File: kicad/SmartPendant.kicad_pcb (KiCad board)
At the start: 2 copper layers, 125 x 59 mm, 51 parts, among them J1 UART, J2 ST-LINK, J3 Encoder, J5 Display, J6 USB_C_Receptacle_USB2.0_16P, J8 Micro_SD_Card_Det1, Q1 MMBT3904, U1 WEACT BLACKPILL F4X1, U2 AMS1117-3.3, U3 MB85RC256VPNF-G-JNERE1

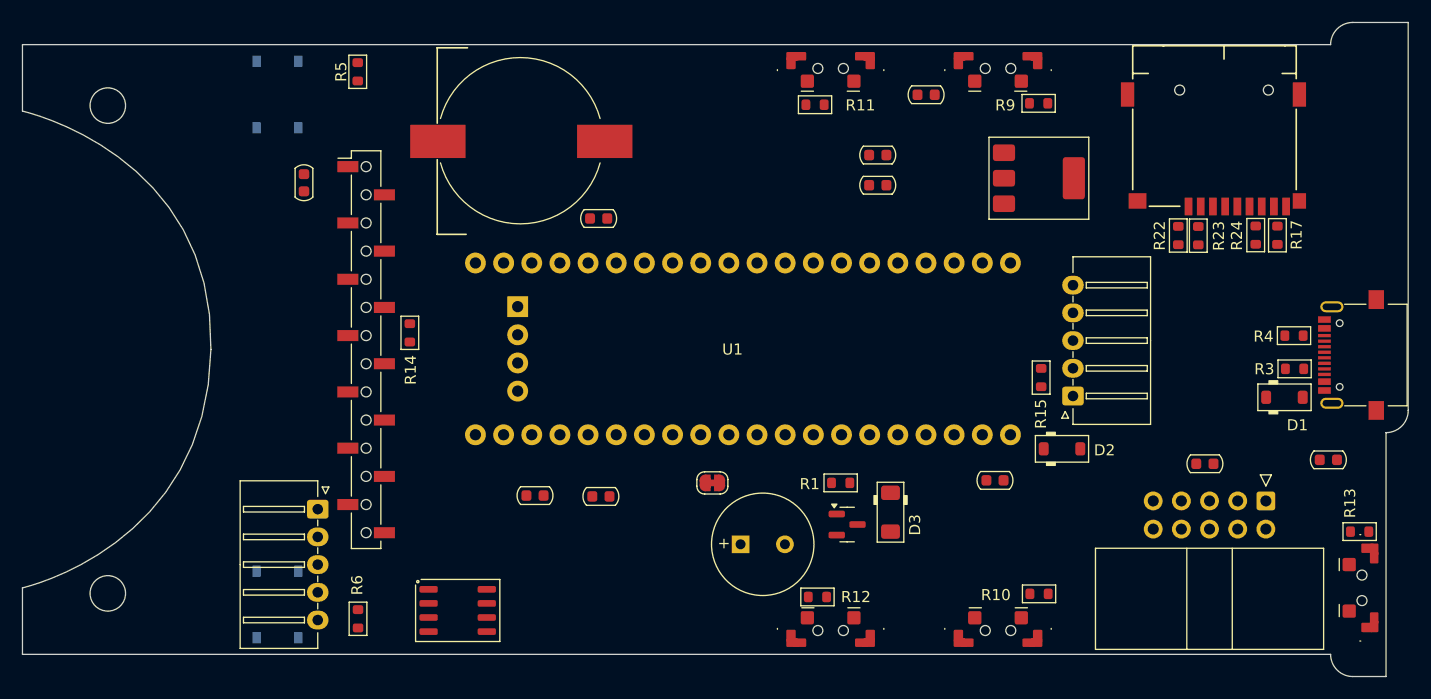
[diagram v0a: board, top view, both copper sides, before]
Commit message: Make PCB wider.
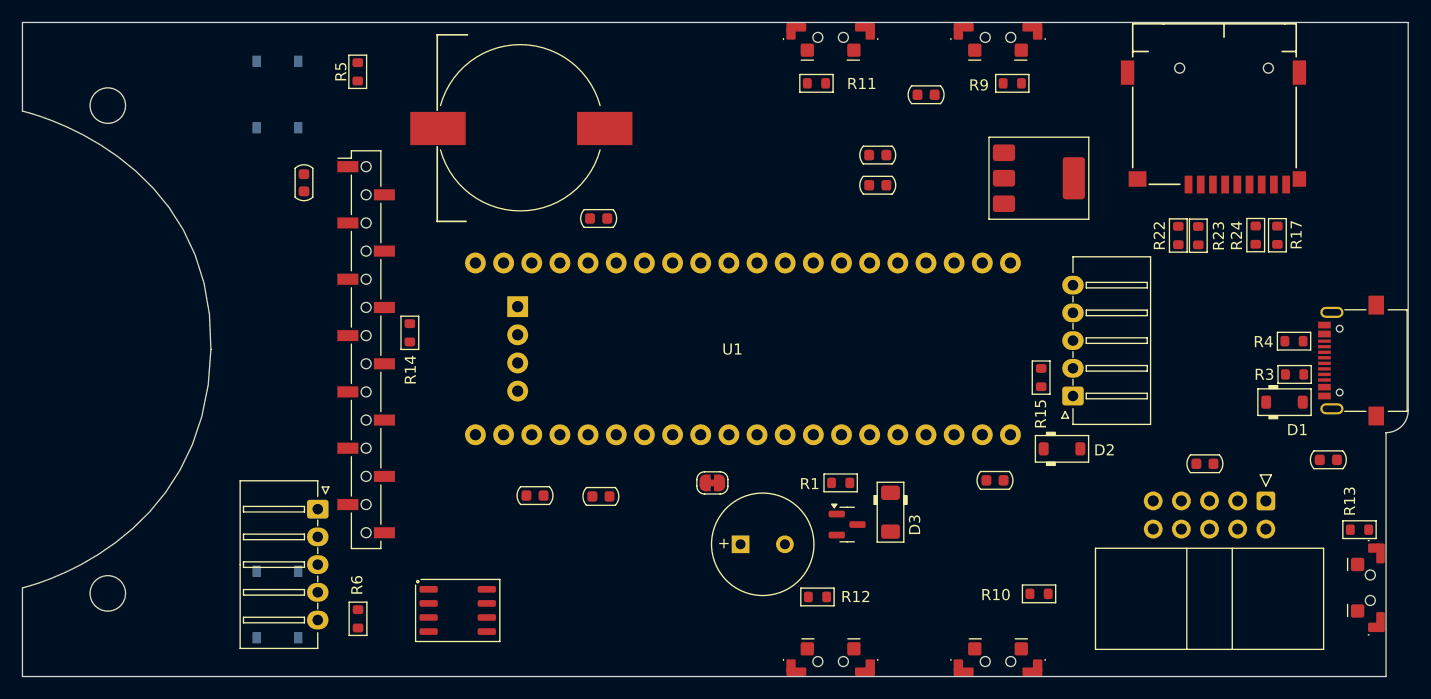
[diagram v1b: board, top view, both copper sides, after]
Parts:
- moved R9 2.98 mm to (214.3, 53.5)
- moved BTN_RD1 2.80 mm to (197.9, 104.9)
- moved BTN_RU1 2.80 mm to (213.0, 104.9)
- moved BTN_LD1 2.80 mm to (197.9, 50.1)
- moved BTN_LU1 2.80 mm to (213.0, 50.1)
- moved J8 1.98 mm to (233.4, 55.6)
- moved R11 1.93 mm to (196.6, 53.5)
- moved BT1 1.17 mm to (169.9, 57.5)
- moved BTN_USR1 0.75 mm to (245.8, 99.0)
- moved R3 0.50 mm to (239.8, 79.8)
- moved J6 0.50 mm to (246.1, 78.5)
- moved R4 0.50 mm to (239.7, 76.8)
- moved D1 0.44 mm to (238.8, 82.2)
- moved R13 0.18 mm to (245.6, 93.8)
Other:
- outline, holes or cut-outs redrawn

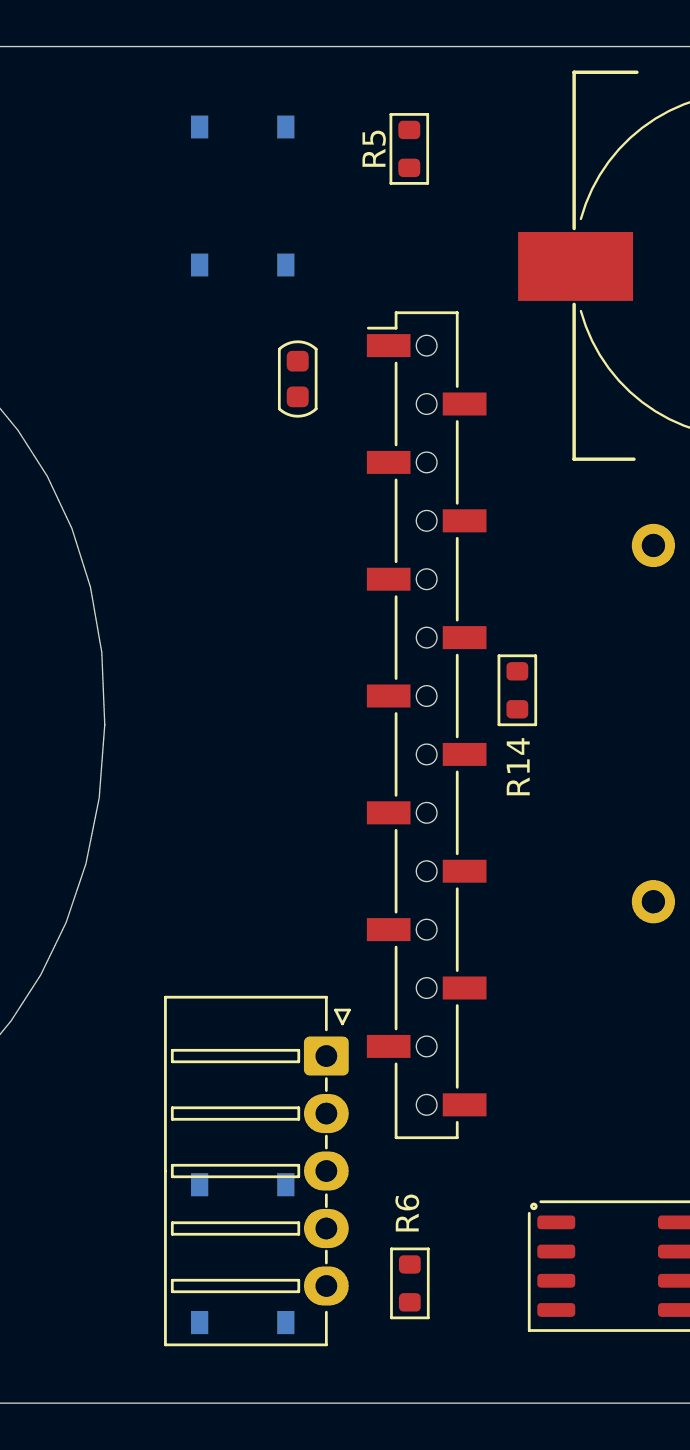
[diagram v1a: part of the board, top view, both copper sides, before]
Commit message: Change front buttons.
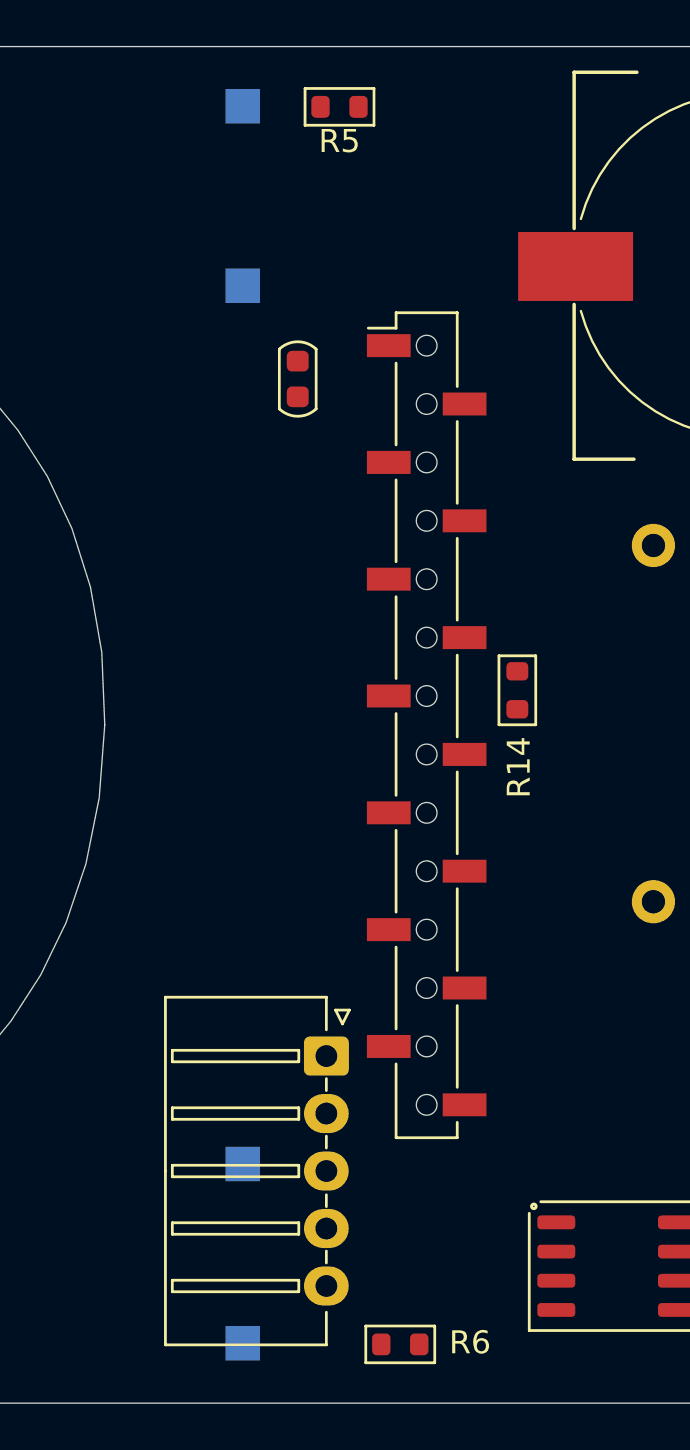
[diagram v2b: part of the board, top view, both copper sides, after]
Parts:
- BTN_L1, BTN_R1: footprint Button_Switch_SMD:SW_Push_1P1T_XKB_TS-1187A -> Button_Switch_SMD:SW_SPST_CK_RS282G05A3
- moved R5 3.54 mm to (152.2, 50.6), turned to 180 degrees
- moved R6 2.69 mm to (154.9, 104.4), turned to 180 degrees
- turned BTN_R1 to 90 degrees

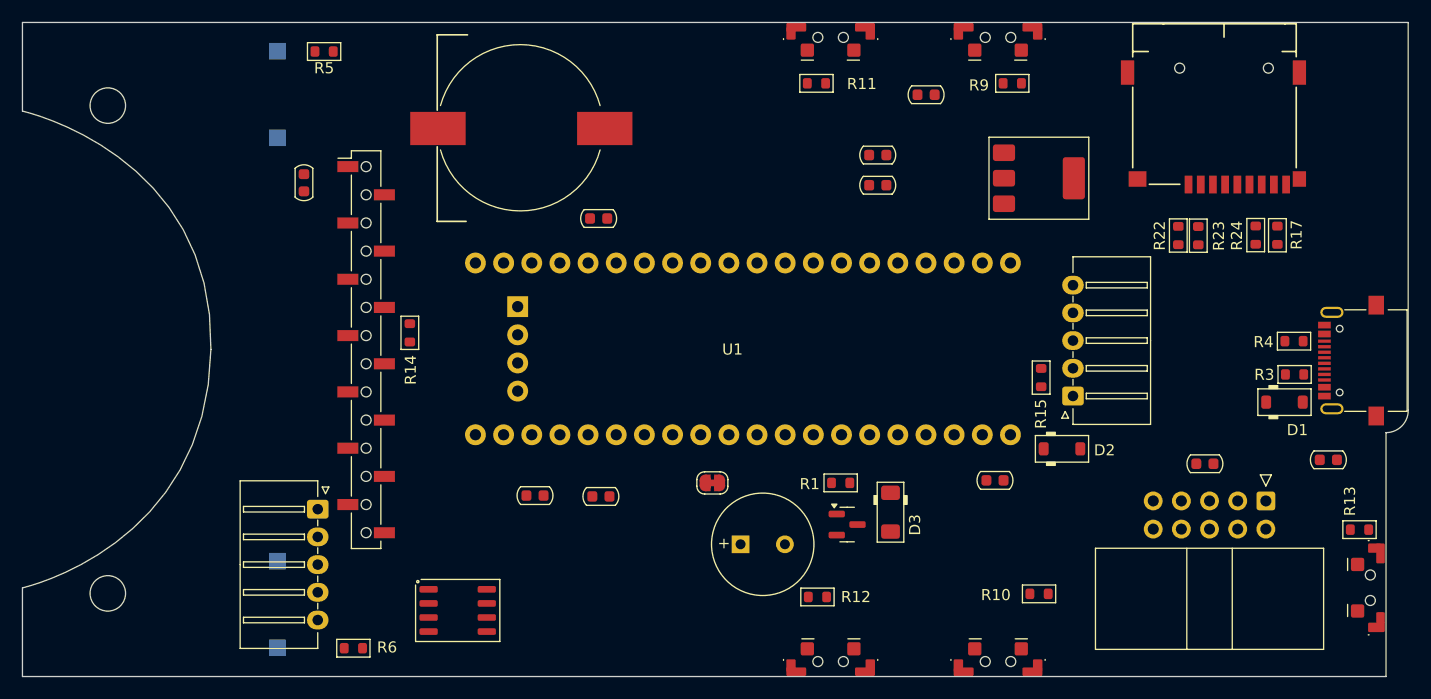
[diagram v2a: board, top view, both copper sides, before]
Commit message: Correct last footprints.
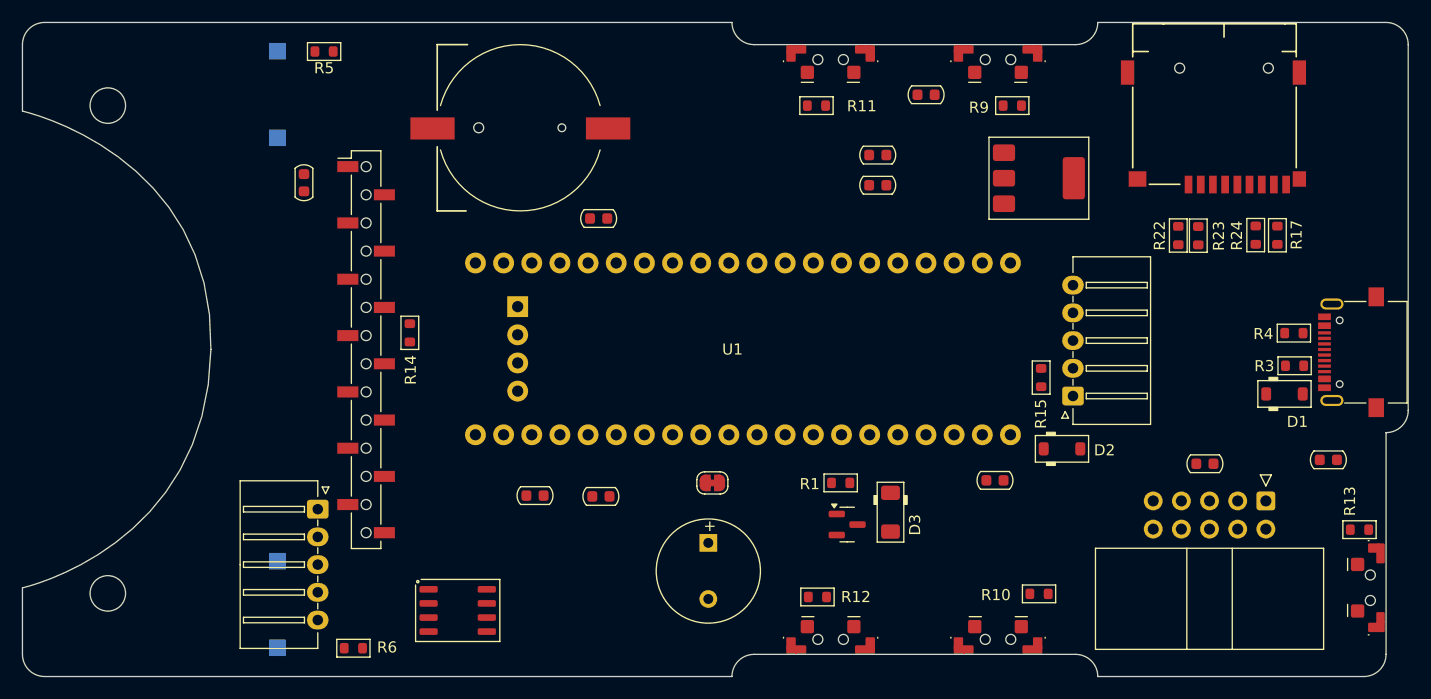
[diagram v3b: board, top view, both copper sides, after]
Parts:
- BZ1: footprint Buzzer_Beeper:MagneticBuzzer_PUI_AT-0927-TT-6-R -> Custom:Buzzer_4.7x9.4mm
- moved BZ1 2.91 mm to (186.9, 94.9), turned to -90 degrees
- moved R11 2.01 mm to (196.6, 55.5)
- moved R9 2.01 mm to (214.3, 55.5)
- moved BTN_LD1 2.00 mm to (197.9, 52.1)
- moved BTN_LU1 2.00 mm to (213.0, 52.1)
- moved BTN_RD1 2.00 mm to (197.9, 102.9)
- moved BTN_RU1 2.00 mm to (213.0, 102.9)
- moved R3 0.78 mm to (239.8, 79.0)
- moved J6 0.75 mm to (246.1, 77.8)
- moved D1 0.74 mm to (238.8, 81.5)
- moved R4 0.73 mm to (239.7, 76.0)
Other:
- outline, holes or cut-outs redrawn
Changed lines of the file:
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@@
 	(footprint "Custom:SMD_Push_Side_button_3x6x3.5mm"
 		(layer "F.Cu")
-		(at 197.9 50.1 180)
+		(at 197.9 52.1 180)
 		(descr "Microminiature SMT Side Actuated, 4.2 x 2.8 x 1.42mm with pegs, https://www.ckswitches.com/media/1482/kms.pdf")
 		(tags "Switch SPST KMS2")
@@
 	(footprint "PCM_Resistor_SMD_AKL:R_0603_1608Metric"
 		(layer "F.Cu")
-		(at 239.6998 76.75 180)
+		(at 239.6876 76.0222 180)
 		(descr "Resistor SMD 0603 (1608 Metric), square (rectangular) end terminal, IPC_7351 nominal, (Body size source: IPC-SM-782 page 72, https://www.pcb-3d.com/wordpress/wp-content/uploads/ipc-sm-782a_amendment_1_and_2.pdf), Alternate KiCad Library")
 		(tags "resistor")
@@
 	(footprint "Custom:USB_C_Receptacle_AliExpress_16pin"
 		(layer "F.Cu")
-		(at 246.1166 78.5 90)
+		(at 246.1166 77.75 90)
 		(descr "USB Type C, right-angle, SMT, https://datasheet.lcsc.com/szlcsc/1811141824_XKB-Enterprise-U262-161N-4BVC11_C319148.pdf")
 		(tags "USB C Type-C Receptacle SMD")
@@
 		)
 	)
-	(footprint "Buzzer_Beeper:MagneticBuzzer_PUI_AT-0927-TT-6-R"
+	(footprint "Custom:Buzzer_4.7x9.4mm"
 		(layer "F.Cu")
-		(at 189.7766 95.0722)
+		(at 186.8678 94.9452 -90)
 		(descr "Buzzer Magnetic 9mm AT-0927-TT-6-R, http://www.puiaudio.com/pdf/AT-0927-TT-6-R.pdf")
 		(tags "Buzzer Magnetic 9mm AT-0927-TT-6-R")
 		(property "Reference" "BZ1"
-			(at 2 5.5 0)
+			(at 2 5.5 90)
 			(layer "F.SilkS")
 			(hide yes)
@@
 		)
 		(property "Value" "Buzzer"
-			(at 2 7 0)
+			(at 2 7 90)
 			(layer "F.Fab")
+			(hide yes)
 			(effects
 				(font
@@
 		)
 		(property "Datasheet" "~"
-			(at 0 0 0)
+			(at 0 0 270)
 			(unlocked yes)
 			(layer "F.Fab")
@@
 		)
 		(property "Description" "Buzzer, polarized"
-			(at 0 0 0)
+			(at 0 0 270)
 			(unlocked yes)
 			(layer "F.Fab")
@@
 		(attr through_hole)
 		(fp_circle
-			(center 2 0)
-			(end 6.62 0)
+			(center 2.54 0)
+			(end 7.24 0)
 			(stroke
 				(width 0.12)
@@
 		)
 		(fp_circle
-			(center 2 0)
-			(end 6.75 0)
+			(center 2.54 0)
+			(end 7.34 0)
 			(stroke
 				(width 0.05)
@@
 		)
 		(fp_circle
-			(center 2 0)
-			(end 6.5 0)
+			(center 2.54 0)
+			(end 7.14 0)
 			(stroke
 				(width 0.1)
@@
 		)
 		(fp_text user "+"
-			(at -1.5 -0.1 0)
+			(at -1.5 -0.1 90)
 			(layer "F.SilkS")
 			(effects
@@
 		)
 		(fp_text user "${REFERENCE}"
-			(at 2 2 0)
+			(at 2 2 90)
 			(layer "F.Fab")
 			(effects
@@
 		)
 		(fp_text user "+"
-			(at -1.5 -0.1 0)
+			(at -1.5 -0.1 90)
 			(layer "F.Fab")
 			(effects
@@
 		)
 		(pad "1" thru_hole rect
-			(at 0 0)
+			(at 0 0 270)
 			(size 1.6 1.6)
 			(drill 0.9)
@@
 		)
 		(pad "2" thru_hole circle
-			(at 4 0)
+			(at 5.06 0 270)
 			(size 1.6 1.6)
 			(drill 0.9)
@@
 	(footprint "PCM_Resistor_SMD_AKL:R_0603_1608Metric"
 		(layer "F.Cu")
-		(at 196.6214 53.4924 180)
+		(at 196.6214 55.5 180)
 		(descr "Resistor SMD 0603 (1608 Metric), square (rectangular) end terminal, IPC_7351 nominal, (Body size source: IPC-SM-782 page 72, https://www.pcb-3d.com/wordpress/wp-content/uploads/ipc-sm-782a_amendment_1_and_2.pdf), Alternate KiCad Library")
 		(tags "resistor")
@@
 	(footprint "Custom:SMD_Push_Side_button_3x6x3.5mm"
 		(layer "F.Cu")
-		(at 197.9 104.9)
+		(at 197.9 102.9)
 		(descr "Microminiature SMT Side Actuated, 4.2 x 2.8 x 1.42mm with pegs, https://www.ckswitches.com/media/1482/kms.pdf")
 		(tags "Switch SPST KMS2")
@@
 	(footprint "PCM_Diode_SMD_AKL:D_SOD-123"
 		(layer "F.Cu")
-		(at 238.8372 82.25)
+		(at 238.8372 81.5086)
 		(descr "SOD-123, Alternate KiCad Library")
 		(tags "SOD-123")
@@
 	(footprint "Custom:SMD_Push_Side_button_3x6x3.5mm"
 		(layer "F.Cu")
-		(at 213 104.9)
+		(at 213 102.9)
 		(descr "Microminiature SMT Side Actuated, 4.2 x 2.8 x 1.42mm with pegs, https://www.ckswitches.com/media/1482/kms.pdf")
 		(tags "Switch SPST KMS2")
@@
 	(footprint "PCM_Resistor_SMD_AKL:R_0603_1608Metric"
 		(layer "F.Cu")
-		(at 214.2866 53.4924)
+		(at 214.2866 55.5)
 		(descr "Resistor SMD 0603 (1608 Metric), square (rectangular) end terminal, IPC_7351 nominal, (Body size source: IPC-SM-782 page 72, https://www.pcb-3d.com/wordpress/wp-content/uploads/ipc-sm-782a_amendment_1_and_2.pdf), Alternate KiCad Library")
 		(tags "resistor")
@@
 		(attr through_hole)
 		(fp_line
-			(start -8.382 7.493)
-			(end -8.382 4.7625)
+			(start -7.5 7.493)
+			(end -7.5 4.7625)
 			(stroke
 				(width 0.15)
@@
 		(fp_line
 			(start -1.5875 7.493)
-			(end -8.382 7.493)
+			(end -7.5 7.493)
 			(stroke
 				(width 0.15)
@@
 		(fp_line
 			(start 1.7145 7.493)
-			(end 8.4455 7.493)
+			(end 7.5 7.493)
 			(stroke
 				(width 0.15)
@@
 		)
 		(fp_line
-			(start 8.4455 7.493)
-			(end 8.4455 4.8895)
+			(start 7.5 7.493)
+			(end 7.5 4.8895)
 			(stroke
 				(width 0.15)
@@
 			(layer "F.SilkS")
 		)
+		(pad "" np_thru_hole circle
+			(at 0 -3.75 270)
+			(size 0.7 0.7)
+			(drill 0.7)
+			(layers "*.Cu" "*.Mask")
+			(thermal_bridge_angle 90)
+		)
+		(pad "" np_thru_hole circle
+			(at 0 3.75 270)
+			(size 0.9 0.9)
+			(drill 0.9)
+			(layers "*.Cu" "*.Mask")
+			(thermal_bridge_angle 90)
+		)
 		(pad "1" smd rect
-			(at 0.0635 7.4295 270)
-			(size 3 5)
+			(at 0.0635 7.92 270)
+			(size 2 4)
 			(layers "F.Cu" "F.Mask" "F.Paste")
 			(net 55 "BAT")
@@
 		)
 		(pad "2" smd rect
-			(at 0.0635 -7.62 270)
-			(size 3 5)
+			(at 0.0635 -7.92 270)
+			(size 2 4)
 			(layers "F.Cu" "F.Mask" "F.Paste")
 			(net 1 "GND")
@@
 	(footprint "Custom:SMD_Push_Side_button_3x6x3.5mm"
 		(layer "F.Cu")
-		(at 213 50.1 180)
+		(at 213 52.1 180)
 		(descr "Microminiature SMT Side Actuated, 4.2 x 2.8 x 1.42mm with pegs, https://www.ckswitches.com/media/1482/kms.pdf")
 		(tags "Switch SPST KMS2")
@@
 	(footprint "PCM_Resistor_SMD_AKL:R_0603_1608Metric"
 		(layer "F.Cu")
-		(at 239.7506 79.75 180)
+		(at 239.7506 78.9686 180)
 		(descr "Resistor SMD 0603 (1608 Metric), square (rectangular) end terminal, IPC_7351 nominal, (Body size source: IPC-SM-782 page 72, https://www.pcb-3d.com/wordpress/wp-content/uploads/ipc-sm-782a_amendment_1_and_2.pdf), Alternate KiCad Library")
 		(tags "resistor")
@@
 		)
 	)
-	(gr_line
-		(start 225.8568 111.5568)
-		(end 225.9076 46.2026)
+	(gr_arc
+		(start 191 50)
+		(mid 189.585786 49.414214)
+		(end 189 48)
 		(stroke
-			(width 0.1)
-			(type default)
+			(width 0.05)
+			(type solid)
 		)
-		(layer "Dwgs.User")
+		(layer "Edge.Cuts")
+	)
+	(gr_arc
+		(start 127 107)
+		(mid 125.585786 106.414214)
+		(end 125 105)
+		(stroke
+			(width 0.05)
+			(type solid)
+		)
+		(layer "Edge.Cuts")
 	)
 	(gr_line
 		(start 125 99)
-		(end 125 107)
+		(end 125 105)
 		(stroke
 			(width 0.049999)
@@
 	(gr_line
 		(start 248 85)
-		(end 248 107)
+		(end 248 105)
+		(stroke
+			(width 0.05)
+			(type solid)
+		)
+		(layer "Edge.Cuts")
+	)
+	(gr_arc
+		(start 220 105)
+		(mid 221.414214 105.585786)
+		(end 222 107)
+		(stroke
+			(width 0.05)
+			(type solid)
+		)
+		(layer "Edge.Cuts")
+	)
+	(gr_line
+		(start 191 50)
+		(end 220 50)
 		(stroke
 			(width 0.05)
@@
 	)
 	(gr_line
-		(start 125 48)
-		(end 250 48)
+		(start 127 48)
+		(end 189 48)
 		(stroke
 			(width 0.05)
@@
 	)
 	(gr_line
-		(start 250 48)
+		(start 250 50)
 		(end 250 83)
 		(stroke
@@
 		(layer "Edge.Cuts")
 	)
+	(gr_arc
+		(start 189 107)
+		(mid 189.585786 105.585786)
+		(end 191 105)
+		(stroke
+			(width 0.05)
+			(type solid)
+		)
+		(layer "Edge.Cuts")
+	)
+	(gr_line
+		(start 222 48)
+		(end 248 48)
+		(stroke
+			(width 0.05)
+			(type solid)
+		)
+		(layer "Edge.Cuts")
+	)
 	(gr_curve
 		(pts
@@
 		(layer "Edge.Cuts")
 	)
+	(gr_arc
+		(start 248 105)
+		(mid 247.414214 106.414214)
+		(end 246 107)
+		(stroke
+			(width 0.05)
+			(type solid)
+		)
+		(layer "Edge.Cuts")
+	)
 	(gr_line
-		(start 125 48)
-		(end 125 55.998154)
+		(start 125 50)
+		(end 125 56)
 		(stroke
 			(width 0.049999)
@@
 	(gr_curve
 		(pts
-			(xy 125 55.998154) (xy 125 55.998154) (xy 142.37674 59.840307) (xy 141.999998 77.50008)
+			(xy 125 56) (xy 125 55.998154) (xy 142.37674 59.840307) (xy 141.999998 77.50008)
 		)
 		(stroke
@@
 	)
 	(gr_line
-		(start 125 107)
-		(end 248 107)
+		(start 127 107)
+		(end 189 107)
+		(stroke
+			(width 0.05)
+			(type solid)
+		)
+		(layer "Edge.Cuts")
+	)
+	(gr_arc
+		(start 125 50)
+		(mid 125.585786 48.585786)
+		(end 127 48)
+		(stroke
+			(width 0.05)
+			(type solid)
+		)
+		(layer "Edge.Cuts")
+	)
+	(gr_line
+		(start 222 107)
+		(end 246 107)
 		(stroke
 			(width 0.05)
@@
 		(stroke
 			(width 0.05)
+			(type solid)
+		)
+		(layer "Edge.Cuts")
+	)
+	(gr_arc
+		(start 248 48)
+		(mid 249.414214 48.585786)
+		(end 250 50)
+		(stroke
+			(width 0.05)
+			(type solid)
+		)
+		(layer "Edge.Cuts")
+	)
+	(gr_arc
+		(start 222 48)
+		(mid 221.414214 49.414214)
+		(end 220 50)
+		(stroke
+			(width 0.05)
+			(type solid)
+		)
+		(layer "Edge.Cuts")
+	)
+	(gr_line
+		(start 191 105)
+		(end 220 105)
+		(stroke
+			(width 0.05)
